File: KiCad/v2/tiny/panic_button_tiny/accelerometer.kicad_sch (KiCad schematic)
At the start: 1 part, among them U3 LIS2DE12

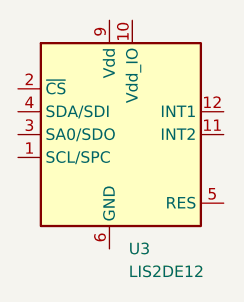
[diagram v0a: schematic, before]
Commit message: [UPDATE] the structure of the KiCad design for the tiny version
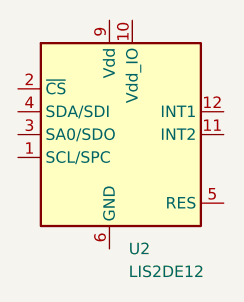
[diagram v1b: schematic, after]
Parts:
- renumbered U3 to U2
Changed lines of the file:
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@@
 		(dnp no)
 		(fields_autoplaced yes)
-		(property "Reference" "U3"
+		(property "Reference" "U2"
 			(at 41.5133 49.53 0)
 			(show_name no)
@@
 			(project "panic_button_tiny"
 				(path "/c4eb92e9-b42f-4db0-b1d9-0ef70f7ca601/808748e4-79b9-4201-99f3-f752df4bbb35"
-					(reference "U3")
+					(reference "U2")
 					(unit 1)
 				)

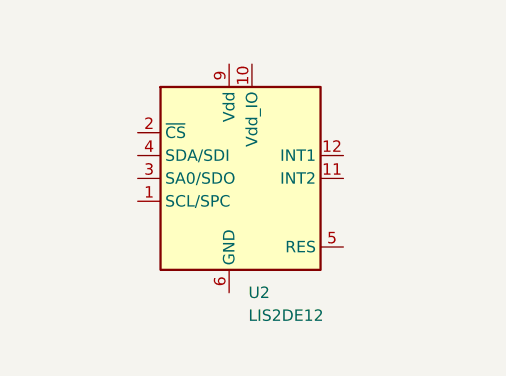
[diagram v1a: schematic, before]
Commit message: [ADD] GND symbols to obvious locations requirering it
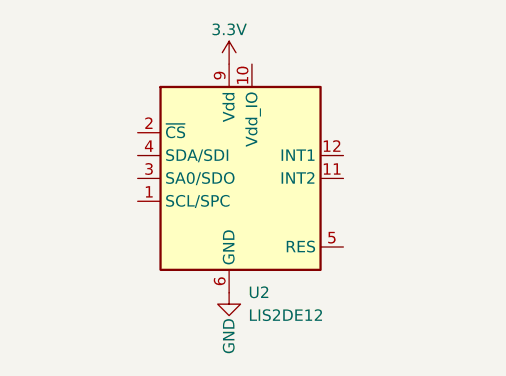
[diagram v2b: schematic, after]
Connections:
- net GND: now reaches U2.6 (GND), U2.7 (GND), U2.8 (GND)
- net 3.3V: now reaches U2.9 (Vdd)
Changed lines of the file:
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@@
+		)
+	)
+	(symbol
+		(lib_id "PCM_SparkFun-PowerSymbol:3.3V")
+		(at 39.37 24.13 0)
+		(unit 1)
+		(body_style 1)
+		(exclude_from_sim no)
+		(in_bom yes)
+		(on_board yes)
+		(in_pos_files yes)
+		(dnp no)
+		(fields_autoplaced yes)
+		(property "Reference" "#PWR050"
+			(at 39.37 27.94 0)
+			(hide yes)
+			(show_name no)
+			(do_not_autoplace no)
+			(effects
+				(font
+					(size 1.27 1.27)
+				)
+			)
+		)
+		(property "Value" "3.3V"
+			(at 39.37 20.32 0)
+			(show_name no)
+			(do_not_autoplace yes)
+			(effects
+				(font
+					(size 1.27 1.27)
+				)
+			)
+		)
+		(property "Footprint" ""
+			(at 39.37 24.13 0)
+			(hide yes)
+			(show_name no)
+			(do_not_autoplace no)
+			(effects
+				(font
+					(size 1.27 1.27)
+				)
+			)
+		)
+		(property "Datasheet" ""
+			(at 39.37 24.13 0)
+			(hide yes)
+			(show_name no)
+			(do_not_autoplace no)
+			(effects
+				(font
+					(size 1.27 1.27)
+				)
+			)
+		)
+		(property "Description" "Power symbol creates a global label with name \"3.3V\""
+			(at 39.37 30.48 0)
+			(hide yes)
+			(show_name no)
+			(do_not_autoplace no)
+			(effects
+				(font
+					(size 1.27 1.27)
+				)
+			)
+		)
+		(pin "1"
+		)
+		(instances
+			(project "panic_button_tiny"
+				(path "/c4eb92e9-b42f-4db0-b1d9-0ef70f7ca601/808748e4-79b9-4201-99f3-f752df4bbb35"
+					(reference "#PWR050")
+					(unit 1)
+				)
+			)
+		)
+	)
+	(symbol
+		(lib_id "PCM_SparkFun-PowerSymbol:GND")
+		(at 39.37 49.53 0)
+		(unit 1)
+		(body_style 1)
+		(exclude_from_sim no)
+		(in_bom yes)
+		(on_board yes)
+		(in_pos_files yes)
+		(dnp no)
+		(property "Reference" "#PWR049"
+			(at 39.37 55.88 0)
+			(hide yes)
+			(show_name no)
+			(do_not_autoplace no)
+			(effects
+				(font
+					(size 1.27 1.27)
+				)
+			)
+		)
+		(property "Value" "GND"
+			(at 39.37 54.356 90)
+			(show_name no)
+			(do_not_autoplace yes)
+			(effects
+				(font
+					(size 1.27 1.27)
+				)
+			)
+		)
+		(property "Footprint" ""
+			(at 39.37 49.53 0)
+			(hide yes)
+			(show_name no)
+			(do_not_autoplace no)
+			(effects
+				(font
+					(size 1.27 1.27)
+				)
+			)
+		)
+		(property "Datasheet" ""
+			(at 39.37 49.53 0)
+			(hide yes)
+			(show_name no)
+			(do_not_autoplace no)
+			(effects
+				(font
+					(size 1.27 1.27)
+				)
+			)
+		)
+		(property "Description" "Power symbol creates a global label with name \"GND\" , ground"
+			(at 39.37 58.42 0)
+			(hide yes)
+			(show_name no)
+			(do_not_autoplace no)
+			(effects
+				(font
+					(size 1.27 1.27)
+				)
+			)
+		)
+		(pin "1"
+		)
+		(instances
+			(project "panic_button_tiny"
+				(path "/c4eb92e9-b42f-4db0-b1d9-0ef70f7ca601/808748e4-79b9-4201-99f3-f752df4bbb35"
+					(reference "#PWR049")
+					(unit 1)
+				)
+			)
 		)
 	)

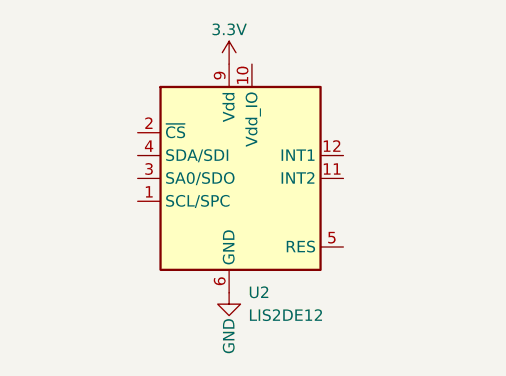
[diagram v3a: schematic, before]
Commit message: [UPDATE] the schematic with a buzzer and wirering for the different components
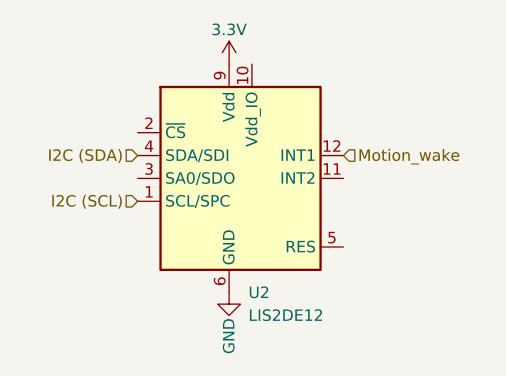
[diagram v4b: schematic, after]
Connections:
- net I2C (SCL): now reaches U2.1 (SCL/SPC)
- net Motion_wake: now reaches U2.12 (INT1)
- net I2C (SDA): now reaches U2.4 (SDA/SDI)
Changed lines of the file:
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@@
 	(generator_version "10.0")
 	(paper "A4")
+	(hierarchical_label "Motion_wake"
+		(shape input)
+		(at 52.07 34.29 0)
+		(effects
+			(font
+				(size 1.27 1.27)
+			)
+			(justify left)
+		)
+	)
+	(hierarchical_label "I2C (SCL)"
+		(shape input)
+		(at 29.21 39.37 180)
+		(effects
+			(font
+				(size 1.27 1.27)
+			)
+			(justify right)
+		)
+	)
+	(hierarchical_label "I2C (SDA)"
+		(shape input)
+		(at 29.21 34.29 180)
+		(effects
+			(font
+				(size 1.27 1.27)
+			)
+			(justify right)
+		)
+	)
 	(symbol
 		(lib_id "Sensor_Motion:LIS2DE12")

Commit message: [UPDATE] the schematic wirering
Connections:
- no-connect marks 0 -> 1
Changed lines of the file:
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@@
 	(generator_version "10.0")
 	(paper "A4")
+	(no_connect
+		(at 52.07 36.83)
+	)
 	(hierarchical_label "Motion_wake"
 		(shape input)
